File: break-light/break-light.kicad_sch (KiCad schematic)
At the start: 75 parts, among them J1 Conn_01x03, J10 Conn_01x08, J11 Conn_01x08, J13 Conn_01x08, J14 Conn_01x08, J15 Conn_01x08, J16 Conn_01x08, J17 Conn_01x08, J3 Conn_01x05, J4 Conn_01x05, J9 Conn_01x08, SW1 SW_SPST, SW2 SW_SPST, U1 STM32F103C8Tx, U2 SN65HVD256D, U4 AP2204K-ADJ, U5 AP63200WU, U6 MAX7219CNG, U7 MAX7219CNG, U8 MAX7219CNG, U9 MAX7219CNG, Y1 8M, Y2 32.768k

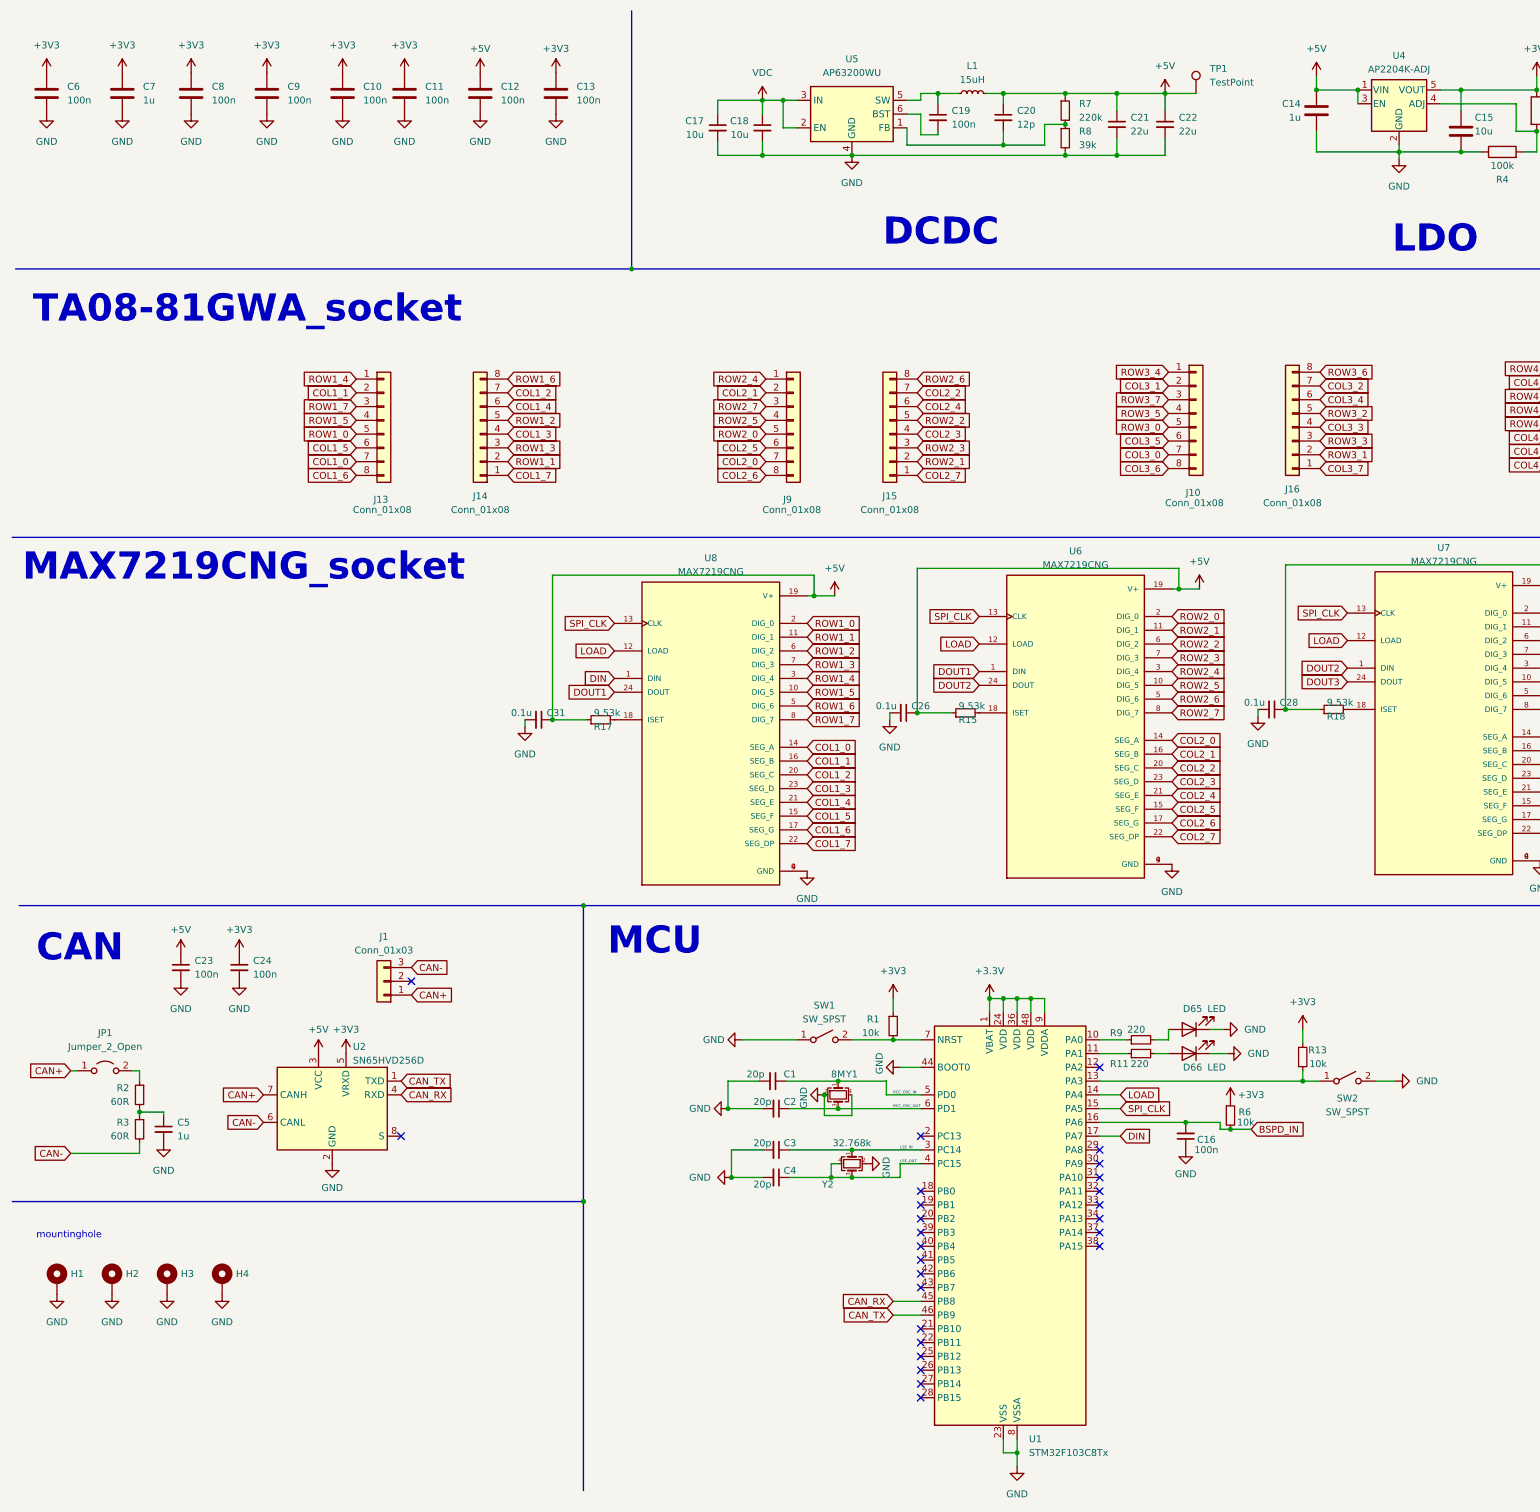
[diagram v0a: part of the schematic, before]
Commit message: fix: re-layout with 4 layers board
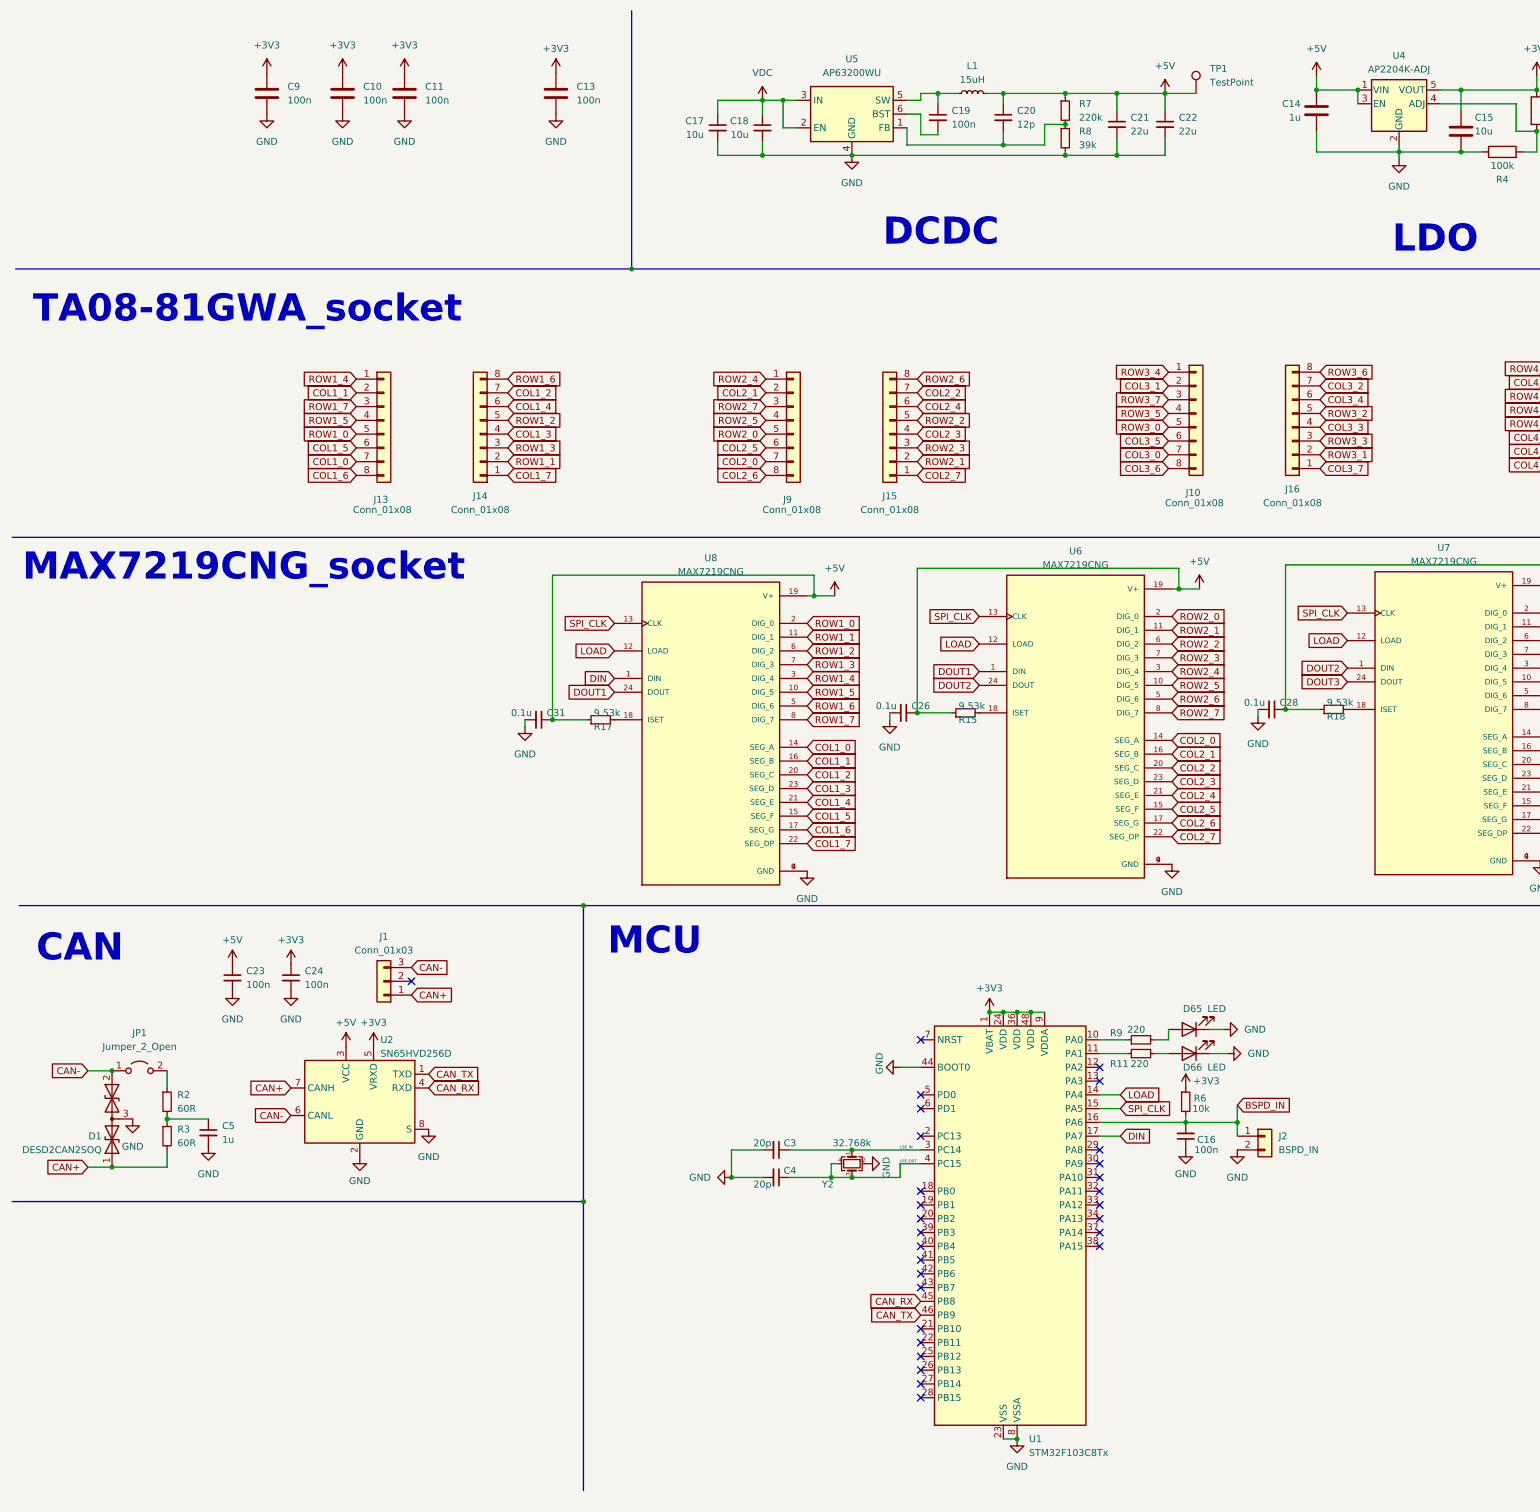
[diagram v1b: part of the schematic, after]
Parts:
- removed C1, C2: 20p, Capacitor_SMD:C_0603_1608Metric, symbol Device:C_Small
- removed C12, C6, C8: 100n, Resistor_SMD:R_0603_1608Metric, symbol Device:C
- removed C7: 1u, Resistor_SMD:R_0603_1608Metric, symbol Device:C
- removed H1, H2, H3, H4: MountingHole_Pad, MountingHole:MountingHole_3.2mm_M3_ISO7380_Pad, symbol Mechanical:MountingHole_Pad
- removed R1, R13: 10k, Resistor_SMD:R_0603_1608Metric, symbol Device:R_Small
- removed SW1, SW2: SW_SPST, Button_Switch_SMD:SW_SPST_FSMSM, symbol Switch:SW_SPST
- removed Y1: 8M, Crystal:Crystal_SMD_SeikoEpson_FA238-4Pin_3.2x2.5mm, symbol Device:Crystal_GND24_Small
- added D1: DESD2CAN2SOQ, Package_TO_SOT_SMD:TSOT-23, symbol Device:D_TVS_Dual_AAC
- added J2: BSPD_IN, Connector_JST:JST_XH_B2B-XH-A_1x02_P2.50mm_Vertical, symbol Connector_Generic:Conn_01x02
- D65, D66: footprint LED_SMD:LED_0603_1608Metric -> LED_SMD:LED_0805_2012Metric
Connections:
- net +3.3V is gone; now on net +3V3: U1.1 (VBAT), U1.24 (VDD), U1.36 (VDD), U1.48 (VDD), U1.9 (VDDA)
- net BSPD_IN: now also J2.1 (Pin_1)
- net CAN+: now also R3.2, D1.1 (A1); no longer JP1.1 (A)
- net CAN-: now also JP1.1 (A), D1.2 (A2); no longer R3.2
- net GND: now also U2.8 (S), D1.3 (common), J2.2 (Pin_2)
- net RCC_OSC_IN: no longer names the net of U1.5 (PD0)
- net RCC_OSC_OUT: no longer names the net of U1.6 (PD1)
- no-connect marks 26 -> 29
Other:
- note removed: "mountinghole"
- moved on the sheet: C23, C24, C5, JP1, R2, R3, R6, U2

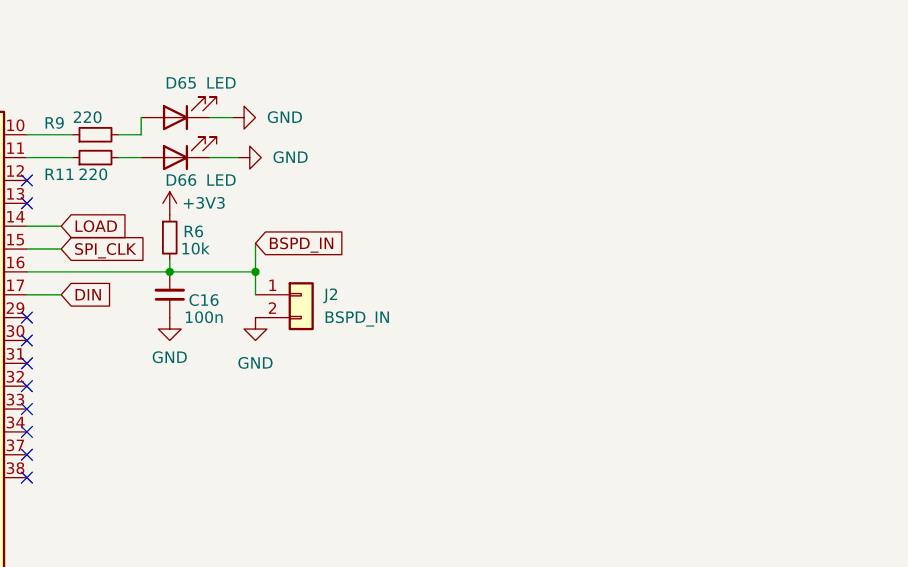
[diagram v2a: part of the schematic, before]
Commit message: feat: add RC filter for brake light
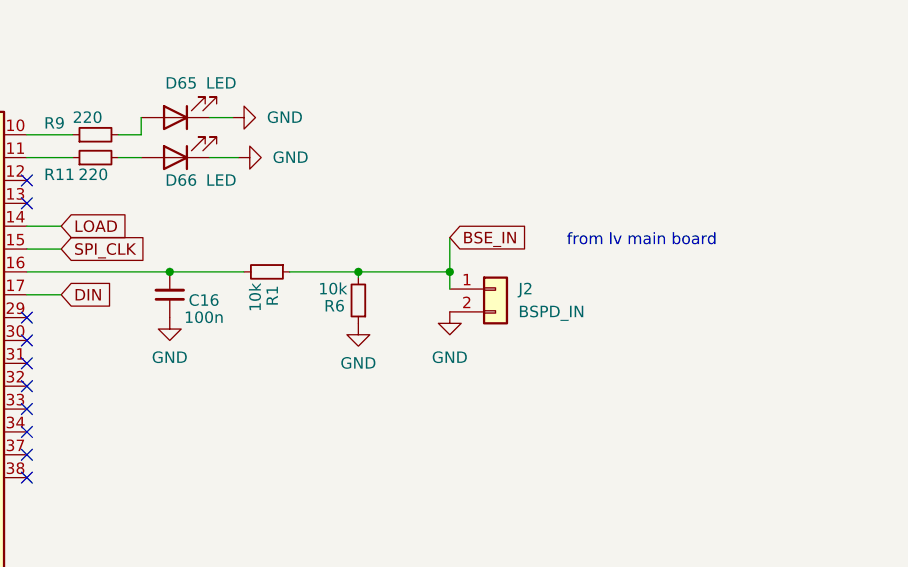
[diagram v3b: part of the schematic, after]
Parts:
- added R1: 10k, Resistor_SMD:R_0603_1608Metric, symbol Device:R_Small
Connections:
- net +3V3: no longer R6.1
- net GND: now also R6.1
- net BSPD_IN: no longer names the net of C16.2, U1.16 (PA6)
- net BSPD_IN: now also R1.2; no longer J2.1 (Pin_1), R6.2
- new net BSE_IN: J2.1 (Pin_1), R1.1, R6.2
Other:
- note added: "from lv main board"
- moved on the sheet: J2, R6

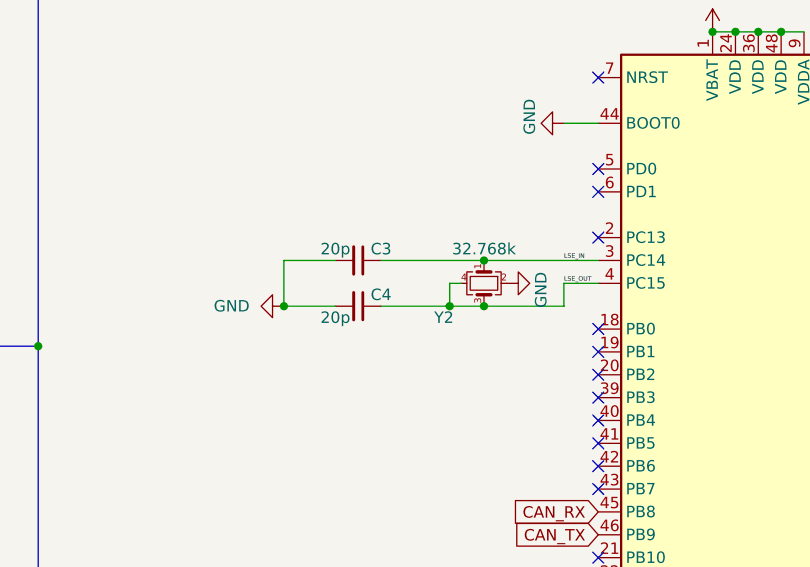
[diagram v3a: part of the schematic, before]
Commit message: feat: flip one side of the LED matrix
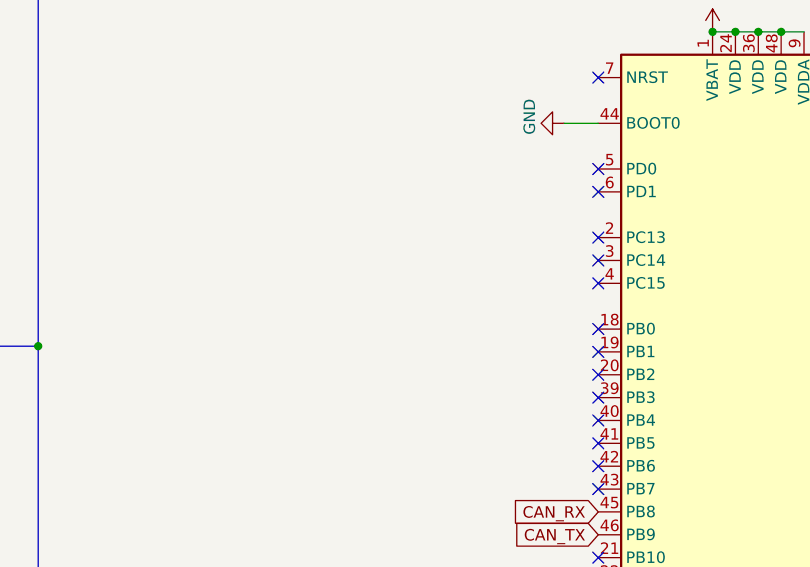
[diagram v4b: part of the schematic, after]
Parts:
- removed C3, C4: 20p, Capacitor_SMD:C_0603_1608Metric, symbol Device:C_Small
- removed Y2: 32.768k, Crystal:Crystal_SMD_SeikoEpson_FA238-4Pin_3.2x2.5mm, symbol Device:Crystal_GND24_Small
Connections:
- net LSE_IN: no longer names the net of U1.3 (PC14)
- net LSE_OUT: no longer names the net of U1.4 (PC15)
- no-connect marks 29 -> 31

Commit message: fix: repair pin
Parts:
- added J5: Conn_01x03, Connector_PinHeader_2.54mm:PinHeader_1x03_P2.54mm_Vertical, symbol Connector_Generic:Conn_01x03
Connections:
- net COL1_0: now also J13.4 (Pin_4), U8.2 (DIG_0); no longer J13.7 (Pin_7), U8.14 (SEG_A)
- net COL1_1: now also J14.6 (Pin_6), U8.11 (DIG_1); no longer J13.2 (Pin_2), U8.16 (SEG_B)
- net COL1_2: now also J14.5 (Pin_5), U8.6 (DIG_2); no longer J14.7 (Pin_7), U8.20 (SEG_C)
- net COL1_3: now also J13.7 (Pin_7), U8.7 (DIG_3); no longer J14.4 (Pin_4), U8.23 (SEG_D)
- net COL1_4: now also J14.3 (Pin_3), U8.3 (DIG_4); no longer J14.6 (Pin_6), U8.21 (SEG_E)
- net COL1_5: now also U8.10 (DIG_5); no longer U8.15 (SEG_F)
- net COL1_6: now also J13.2 (Pin_2), U8.5 (DIG_6); no longer J13.8 (Pin_8), U8.17 (SEG_G)
- net COL1_7: now also J13.1 (Pin_1), U8.8 (DIG_7); no longer J14.1 (Pin_1), U8.22 (SEG_DP)
- net COL2_0: now also J9.4 (Pin_4), U6.2 (DIG_0); no longer J9.7 (Pin_7), U6.14 (SEG_A)
- net COL2_1: now also J15.6 (Pin_6), U6.11 (DIG_1); no longer J9.2 (Pin_2), U6.16 (SEG_B)
- net COL2_2: now also J15.5 (Pin_5), U6.6 (DIG_2); no longer J15.7 (Pin_7), U6.20 (SEG_C)
- net COL2_3: now also J9.7 (Pin_7), U6.7 (DIG_3); no longer J15.4 (Pin_4), U6.23 (SEG_D)
- net COL2_4: now also J15.3 (Pin_3), U6.3 (DIG_4); no longer J15.6 (Pin_6), U6.21 (SEG_E)
- net COL2_5: now also U6.10 (DIG_5); no longer U6.15 (SEG_F)
- net COL2_6: now also J9.2 (Pin_2), U6.5 (DIG_6); no longer J9.8 (Pin_8), U6.17 (SEG_G)
- net COL2_7: now also J9.1 (Pin_1), U6.8 (DIG_7); no longer J15.1 (Pin_1), U6.22 (SEG_DP)
- net COL3_0: now also J10.4 (Pin_4), U7.2 (DIG_0); no longer J10.7 (Pin_7), U7.14 (SEG_A)
- net COL3_1: now also J16.6 (Pin_6), U7.11 (DIG_1); no longer J10.2 (Pin_2), U7.16 (SEG_B)
- net COL3_2: now also J16.5 (Pin_5), U7.6 (DIG_2); no longer J16.7 (Pin_7), U7.20 (SEG_C)
- net COL3_3: now also J10.7 (Pin_7), U7.7 (DIG_3); no longer J16.4 (Pin_4), U7.23 (SEG_D)
- net COL3_4: now also J16.3 (Pin_3), U7.3 (DIG_4); no longer J16.6 (Pin_6), U7.21 (SEG_E)
- net COL3_5: now also U7.10 (DIG_5); no longer U7.15 (SEG_F)
- net COL3_6: now also J10.2 (Pin_2), U7.5 (DIG_6); no longer J10.8 (Pin_8), U7.17 (SEG_G)
- net COL3_7: now also J10.1 (Pin_1), U7.8 (DIG_7); no longer J16.1 (Pin_1), U7.22 (SEG_DP)
- net COL4_0: now also J11.4 (Pin_4), U9.2 (DIG_0); no longer J11.7 (Pin_7), U9.14 (SEG_A)
- net COL4_1: now also J17.6 (Pin_6), U9.11 (DIG_1); no longer J11.2 (Pin_2), U9.16 (SEG_B)
- net COL4_2: now also J17.5 (Pin_5), U9.6 (DIG_2); no longer J17.7 (Pin_7), U9.20 (SEG_C)
- net COL4_3: now also J11.7 (Pin_7), U9.7 (DIG_3); no longer J17.4 (Pin_4), U9.23 (SEG_D)
- net COL4_4: now also J17.3 (Pin_3), U9.3 (DIG_4); no longer J17.6 (Pin_6), U9.21 (SEG_E)
- net COL4_5: now also U9.10 (DIG_5); no longer U9.15 (SEG_F)
- net COL4_6: now also J11.2 (Pin_2), U9.5 (DIG_6); no longer J11.8 (Pin_8), U9.17 (SEG_G)
- net COL4_7: now also J11.1 (Pin_1), U9.8 (DIG_7); no longer J17.1 (Pin_1), U9.22 (SEG_DP)
- net GND: now also J5.3 (Pin_3)
- net ROW1_0: now also J13.8 (Pin_8), U8.14 (SEG_A); no longer J13.5 (Pin_5), U8.2 (DIG_0)
- net ROW1_1: now also J13.3 (Pin_3), U8.16 (SEG_B); no longer J14.2 (Pin_2), U8.11 (DIG_1)
- net ROW1_2: now also J14.1 (Pin_1), U8.20 (SEG_C); no longer J14.5 (Pin_5), U8.6 (DIG_2)
- net ROW1_3: now also J13.5 (Pin_5), U8.23 (SEG_D); no longer J14.3 (Pin_3), U8.7 (DIG_3)
- net ROW1_4: now also J14.8 (Pin_8), U8.21 (SEG_E); no longer J13.1 (Pin_1), U8.3 (DIG_4)
- net ROW1_5: now also J14.2 (Pin_2), U8.15 (SEG_F); no longer J13.4 (Pin_4), U8.10 (DIG_5)
- net ROW1_6: now also J14.7 (Pin_7), U8.17 (SEG_G); no longer J14.8 (Pin_8), U8.5 (DIG_6)
- net ROW1_7: now also J14.4 (Pin_4), U8.22 (SEG_DP); no longer J13.3 (Pin_3), U8.8 (DIG_7)
- net ROW2_0: now also J9.8 (Pin_8), U6.14 (SEG_A); no longer J9.5 (Pin_5), U6.2 (DIG_0)
- net ROW2_1: now also J9.3 (Pin_3), U6.16 (SEG_B); no longer J15.2 (Pin_2), U6.11 (DIG_1)
- net ROW2_2: now also J15.1 (Pin_1), U6.20 (SEG_C); no longer J15.5 (Pin_5), U6.6 (DIG_2)
- net ROW2_3: now also J9.5 (Pin_5), U6.23 (SEG_D); no longer J15.3 (Pin_3), U6.7 (DIG_3)
- net ROW2_4: now also J15.8 (Pin_8), U6.21 (SEG_E); no longer J9.1 (Pin_1), U6.3 (DIG_4)
- net ROW2_5: now also J15.2 (Pin_2), U6.15 (SEG_F); no longer J9.4 (Pin_4), U6.10 (DIG_5)
- net ROW2_6: now also J15.7 (Pin_7), U6.17 (SEG_G); no longer J15.8 (Pin_8), U6.5 (DIG_6)
- net ROW2_7: now also J15.4 (Pin_4), U6.22 (SEG_DP); no longer J9.3 (Pin_3), U6.8 (DIG_7)
- net ROW3_0: now also J10.8 (Pin_8), U7.14 (SEG_A); no longer J10.5 (Pin_5), U7.2 (DIG_0)
- net ROW3_1: now also J10.3 (Pin_3), U7.16 (SEG_B); no longer J16.2 (Pin_2), U7.11 (DIG_1)
- net ROW3_2: now also J16.1 (Pin_1), U7.20 (SEG_C); no longer J16.5 (Pin_5), U7.6 (DIG_2)
- net ROW3_3: now also J10.5 (Pin_5), U7.23 (SEG_D); no longer J16.3 (Pin_3), U7.7 (DIG_3)
- net ROW3_4: now also J16.8 (Pin_8), U7.21 (SEG_E); no longer J10.1 (Pin_1), U7.3 (DIG_4)
- net ROW3_5: now also J16.2 (Pin_2), U7.15 (SEG_F); no longer J10.4 (Pin_4), U7.10 (DIG_5)
- net ROW3_6: now also J16.7 (Pin_7), U7.17 (SEG_G); no longer J16.8 (Pin_8), U7.5 (DIG_6)
- net ROW3_7: now also J16.4 (Pin_4), U7.22 (SEG_DP); no longer J10.3 (Pin_3), U7.8 (DIG_7)
- net ROW4_0: now also J11.8 (Pin_8), U9.14 (SEG_A); no longer J11.5 (Pin_5), U9.2 (DIG_0)
- net ROW4_1: now also J11.3 (Pin_3), U9.16 (SEG_B); no longer J17.2 (Pin_2), U9.11 (DIG_1)
- net ROW4_2: now also J17.1 (Pin_1), U9.20 (SEG_C); no longer J17.5 (Pin_5), U9.6 (DIG_2)
- net ROW4_3: now also J11.5 (Pin_5), U9.23 (SEG_D); no longer J17.3 (Pin_3), U9.7 (DIG_3)
- net ROW4_4: now also J17.8 (Pin_8), U9.21 (SEG_E); no longer J11.1 (Pin_1), U9.3 (DIG_4)
- net ROW4_5: now also J17.2 (Pin_2), U9.15 (SEG_F); no longer J11.4 (Pin_4), U9.10 (DIG_5)
- net ROW4_6: now also J17.7 (Pin_7), U9.17 (SEG_G); no longer J17.8 (Pin_8), U9.5 (DIG_6)
- net ROW4_7: now also J17.4 (Pin_4), U9.22 (SEG_DP); no longer J11.3 (Pin_3), U9.8 (DIG_7)
- net SWDIO: now reaches U1.34 (PA13)
- net SWDIO: now also J5.1 (Pin_1)
- net SWCLK: now reaches U1.37 (PA14)
- net SWCLK: now also J5.2 (Pin_2)
- no-connect marks 31 -> 29
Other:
- moved on the sheet: J10, J11, J13, J14, J15, J16, J17, J9
